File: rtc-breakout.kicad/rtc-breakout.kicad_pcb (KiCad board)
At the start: 2 copper layers, 25.4 x 16.5 mm, 3 parts, among them J1 Pi, J2 RTC, SW1 SW_Push

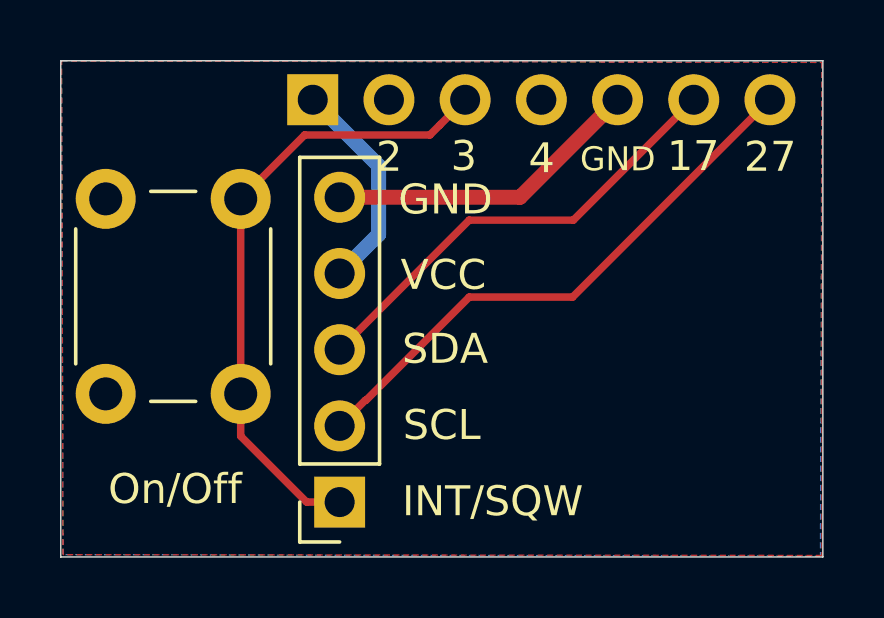
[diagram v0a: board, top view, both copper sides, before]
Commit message: updated labels
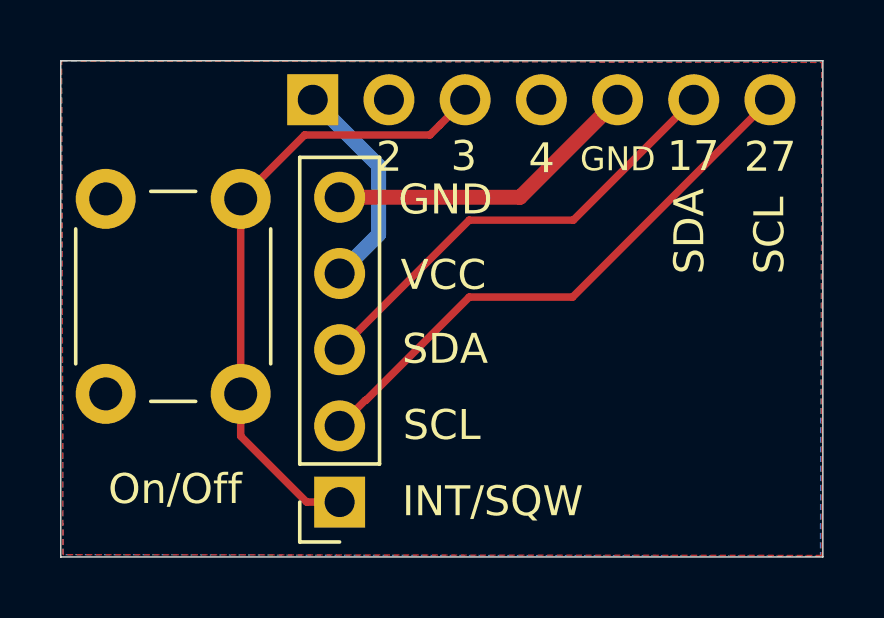
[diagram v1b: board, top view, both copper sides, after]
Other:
- board text added: "Rev: 1b"
- board text removed: "Rev: 1"
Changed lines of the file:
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@@
   (general
     (thickness 1.6)
-    (drawings 18)
+    (drawings 20)
     (tracks 21)
     (zones 0)
@@
     )
   )
+  (gr_text SCL (at 109.474 60.706 90) (layer F.SilkS)
+    (effects (font (size 1 1) (thickness 0.15)) (justify left))
+  )
+  (gr_text SDA (at 106.807 60.706 90) (layer F.SilkS)
+    (effects (font (size 1 1) (thickness 0.15)) (justify left))
+  )
   (gr_text On/Off (at 89.662 67.8688) (layer F.SilkS)
     (effects (font (size 1 1) (thickness 0.15)))
@@
     (effects (font (size 1 1) (thickness 0.15)))
   )
-  (gr_text "Rev: 1" (at 110.8456 69.0626) (layer B.SilkS)
+  (gr_text "Rev: 1b" (at 110.8456 69.0626) (layer B.SilkS)
     (effects (font (size 0.9 0.9) (thickness 0.15)) (justify left mirror))
   )
